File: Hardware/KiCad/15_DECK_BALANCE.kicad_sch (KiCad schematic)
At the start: 0 parts

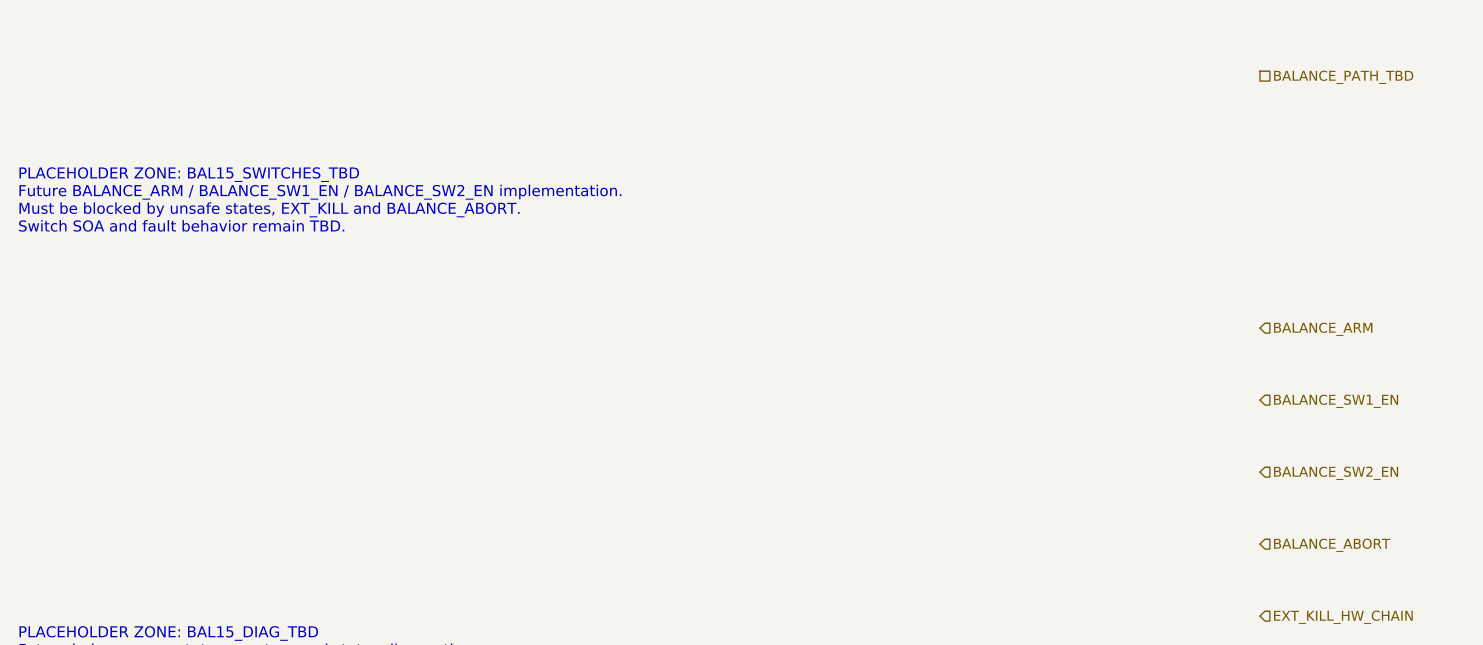
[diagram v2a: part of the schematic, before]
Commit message: hardware: align deck balance control interface
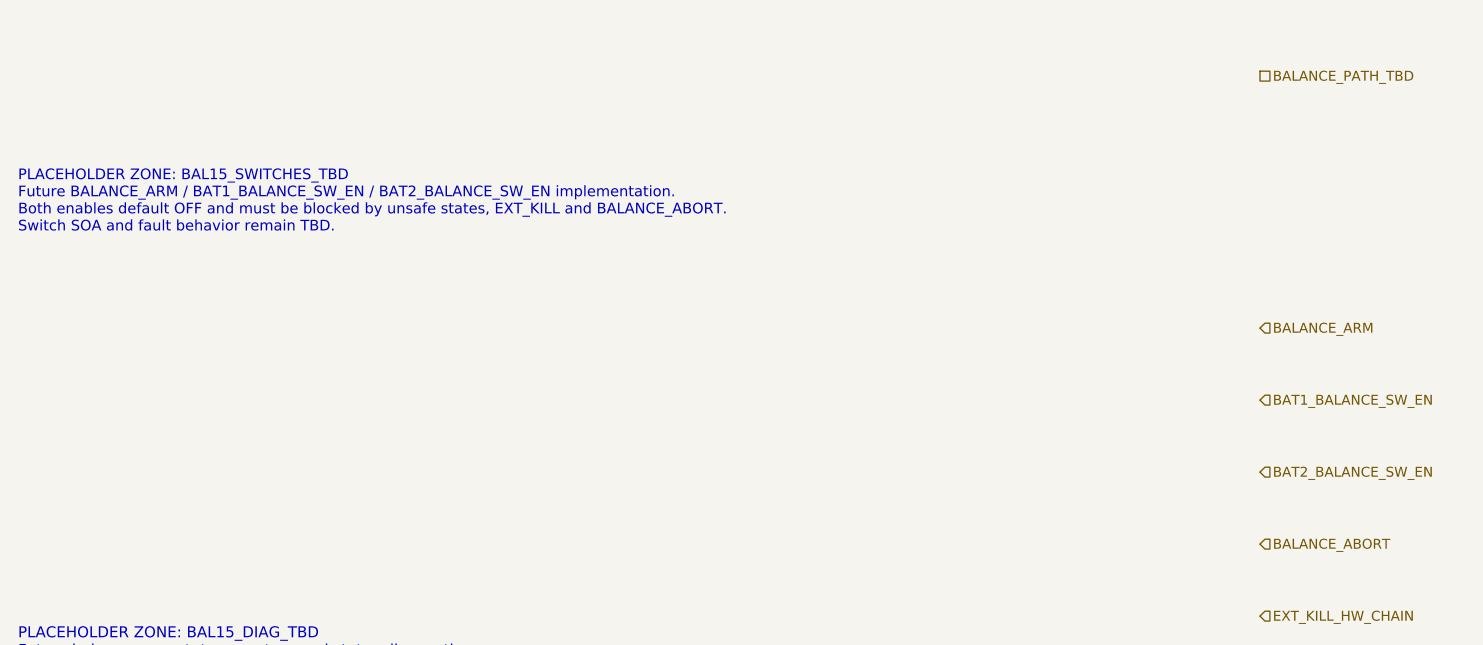
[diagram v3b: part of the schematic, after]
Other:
- note added: "PLACEHOLDER ZONE: BAL15_SWITCHES_TBD Future BALANCE_ARM / BAT1_BALANCE_SW_EN / BAT2_BALANCE_SW_EN implementation. Both enables default OFF and must be blocked by unsafe states, EXT_KILL and BALANCE_ABORT. Switch SOA and fault behavior remain TBD."
- note removed: "PLACEHOLDER ZONE: BAL15_SWITCHES_TBD Future BALANCE_ARM / BALANCE_SW1_EN / BALANCE_SW2_EN implementation. Must be blocked by unsafe states, EXT_KILL and BALANCE_ABORT. Switch SOA and fault behavior remain TBD."
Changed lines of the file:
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@@
 		(title "15_DECK_BALANCE - controlled equalization path")
 		(date "2026-07-15")
-		(rev "C1")
+		(rev "C2")
 		(company "Gonoboben/plataVM")
-		(comment 1 "Symbol skeleton: deck balance switch/resistor/diagnostic placeholders")
+		(comment 1 "Interface consistency: canonical BAT1/BAT2 balance enables")
 		(comment 2 "No resistor value, switch technology, SOA or footprint selected")
 	)
@@
 		(uuid "bfe-lb-00000015-0000-4000-8000-000000000102")
 	)
-	(text "PLACEHOLDER ZONE: BAL15_SWITCHES_TBD\nFuture BALANCE_ARM / BALANCE_SW1_EN / BALANCE_SW2_EN implementation.\nMust be blocked by unsafe states, EXT_KILL and BALANCE_ABORT.\nSwitch SOA and fault behavior remain TBD."
+	(text "PLACEHOLDER ZONE: BAL15_SWITCHES_TBD\nFuture BALANCE_ARM / BAT1_BALANCE_SW_EN / BAT2_BALANCE_SW_EN implementation.\nBoth enables default OFF and must be blocked by unsafe states, EXT_KILL and BALANCE_ABORT.\nSwitch SOA and fault behavior remain TBD."
 		(exclude_from_sim no)
 		(at 12 116 0)
-		(effects (font (size 1.22 1.22)) (justify left))
+		(effects (font (size 1.18 1.18)) (justify left))
 		(uuid "bfe-lb-00000015-0000-4000-8000-000000000103")
 	)
@@
 	(hierarchical_label "BALANCE_PATH_TBD" (shape passive) (exclude_from_sim no) (at 150 102 0) (effects (font (size 1.1 1.1)) (justify left)) (uuid "bfe-lb-00000015-0000-4000-8000-000000000203"))
 	(hierarchical_label "BALANCE_ARM" (shape input) (exclude_from_sim no) (at 150 130 0) (effects (font (size 1.1 1.1)) (justify left)) (uuid "bfe-lb-00000015-0000-4000-8000-000000000204"))
-	(hierarchical_label "BALANCE_SW1_EN" (shape input) (exclude_from_sim no) (at 150 138 0) (effects (font (size 1.1 1.1)) (justify left)) (uuid "bfe-lb-00000015-0000-4000-8000-000000000205"))
-	(hierarchical_label "BALANCE_SW2_EN" (shape input) (exclude_from_sim no) (at 150 146 0) (effects (font (size 1.1 1.1)) (justify left)) (uuid "bfe-lb-00000015-0000-4000-8000-000000000206"))
+	(hierarchical_label "BAT1_BALANCE_SW_EN" (shape input) (exclude_from_sim no) (at 150 138 0) (effects (font (size 1.1 1.1)) (justify left)) (uuid "bfe-lb-00000015-0000-4000-8000-000000000205"))
+	(hierarchical_label "BAT2_BALANCE_SW_EN" (shape input) (exclude_from_sim no) (at 150 146 0) (effects (font (size 1.1 1.1)) (justify left)) (uuid "bfe-lb-00000015-0000-4000-8000-000000000206"))
 	(hierarchical_label "BALANCE_ABORT" (shape input) (exclude_from_sim no) (at 150 154 0) (effects (font (size 1.1 1.1)) (justify left)) (uuid "bfe-lb-00000015-0000-4000-8000-000000000207"))
 	(hierarchical_label "EXT_KILL_HW_CHAIN" (shape input) (exclude_from_sim no) (at 150 162 0) (effects (font (size 1.1 1.1)) (justify left)) (uuid "bfe-lb-00000015-0000-4000-8000-000000000208"))
